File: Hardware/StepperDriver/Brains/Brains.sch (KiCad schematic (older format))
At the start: 14 parts, among them IC1 ATMEGA328-P, P1 CONN_01X02, P2 CONN_01X02, P3 CONN_01X04, P4 CONN_01X04, P5 CONN_01X04, P6 CONN_01X04, Y1 Crystal

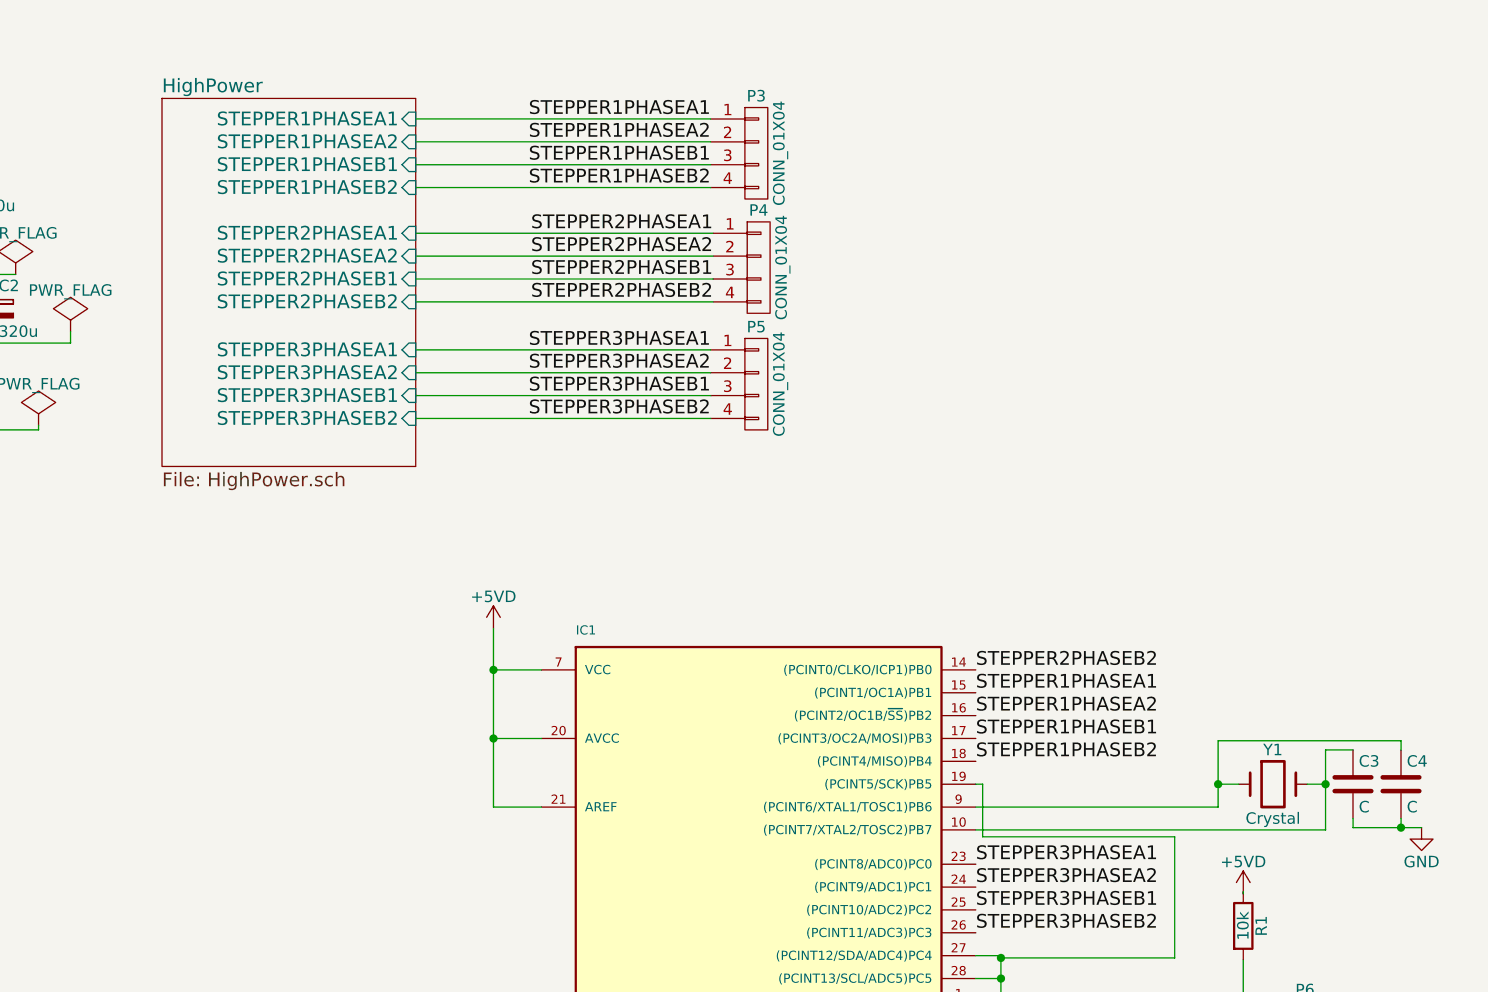
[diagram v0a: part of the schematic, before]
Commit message: updated to modularised design and initial draft of production layout
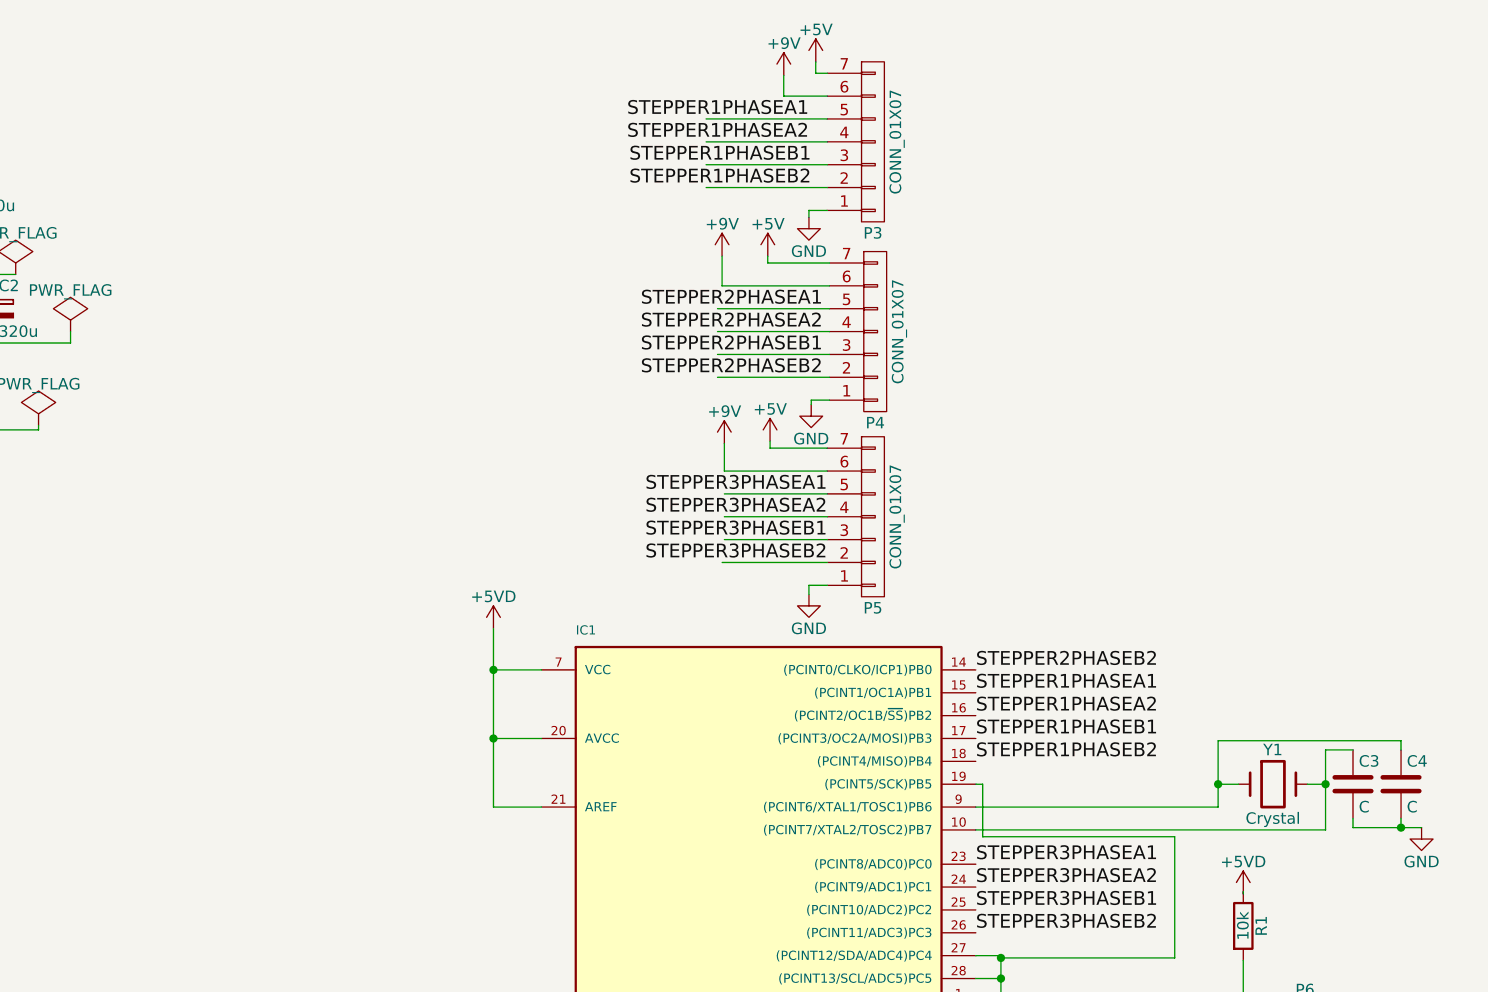
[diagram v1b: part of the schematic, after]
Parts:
- removed P3, P4, P5: CONN_01X04, Terminal_Blocks:TerminalBlock_Pheonix_MPT-2.54mm_4pol, symbol CONN_01X04
- added P3, P4, P5: CONN_01X07, Pin_Headers:Pin_Header_Straight_1x07, symbol CONN_01X07
- P2: footprint Terminal_Blocks:TerminalBlock_Pheonix_MPT-2.54mm_2pol -> Sockets_WAGO734:WAGO_734_2pin_Straight_RuggedPads
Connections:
- wire segments 70 -> 88

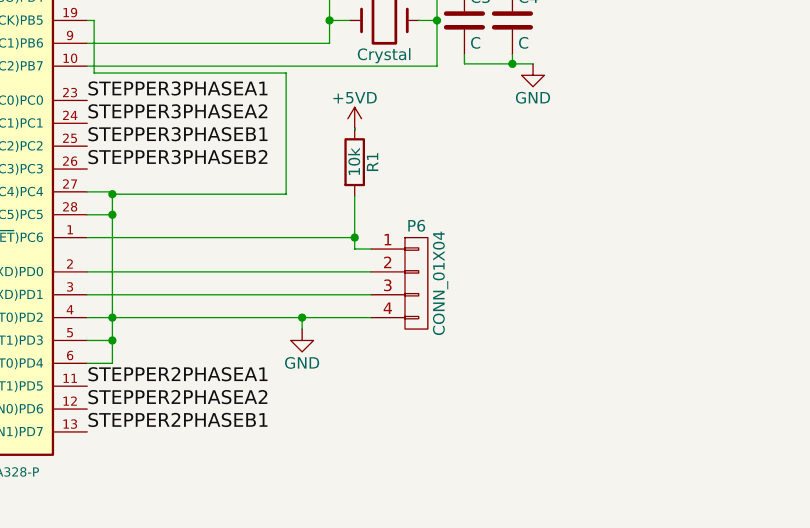
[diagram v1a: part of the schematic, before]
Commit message: various production tweaks: fixed track layers and footprints
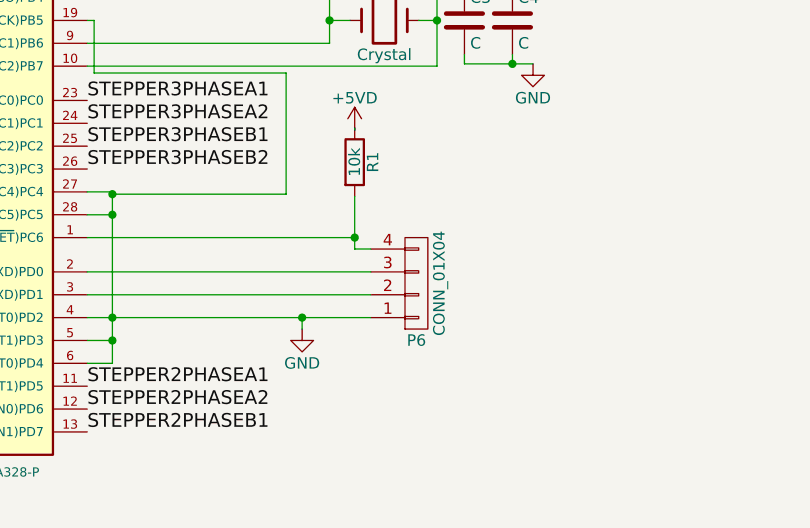
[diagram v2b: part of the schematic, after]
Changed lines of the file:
@@
 F 3 "" H 7350 5000 60  0000 C CNN
 	1    7350 5000
-	1    0    0    -1
+	1    0    0    1
 $EndComp
 $Comp
